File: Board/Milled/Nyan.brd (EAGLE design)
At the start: 86 x 42 mm, 21 parts, among them IC1 74HCT541N, T1 TSM2314CX, U1 BLUEPILL455, U2 A4988_STEP, U3 MAX6966, X1 WR-WTB2.0-2_THT-VER, X2 WR-WTB2.0-4_THT_VER, X3 WR-WTB2.0-4_THT_VER, X4 WR-WTB2.0-5_THT-VER, X6 68610614122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

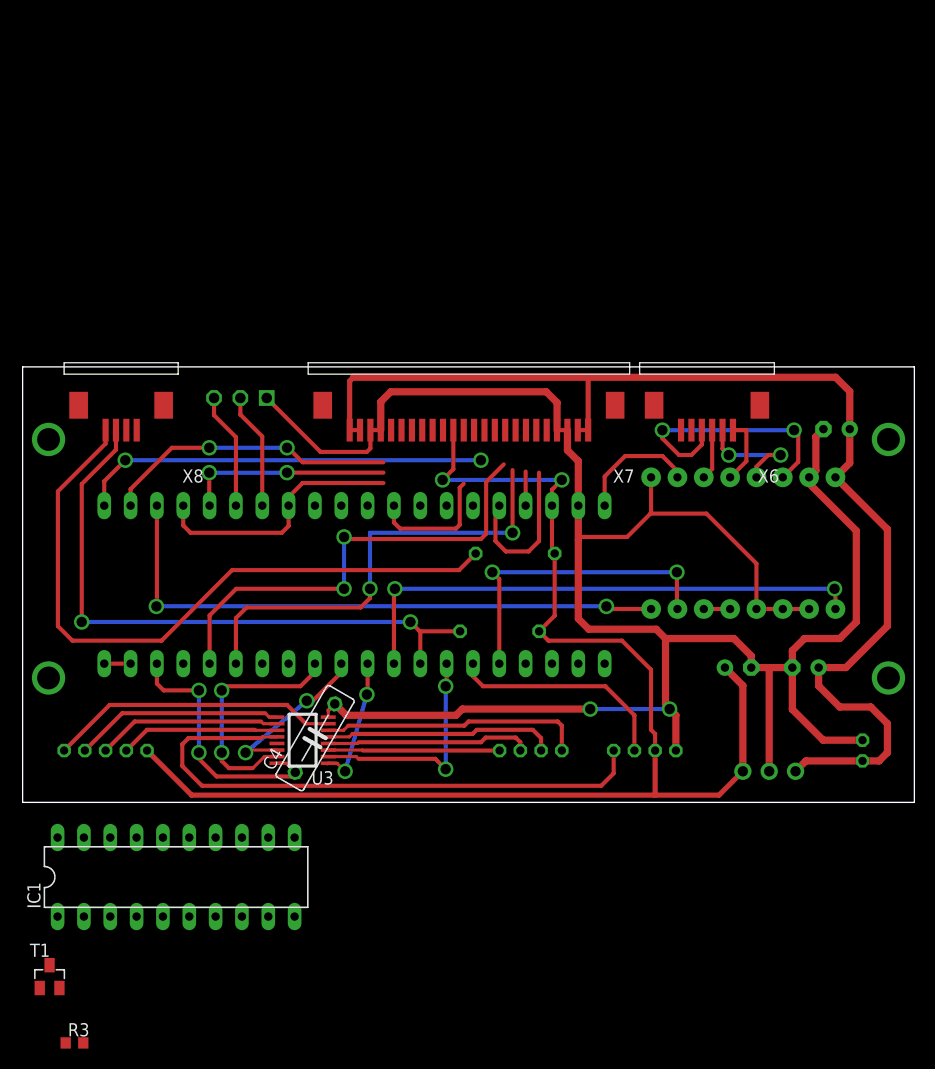
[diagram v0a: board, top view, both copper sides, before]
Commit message: Current development state with hardware fixes for 3 to 5 volt level shifting
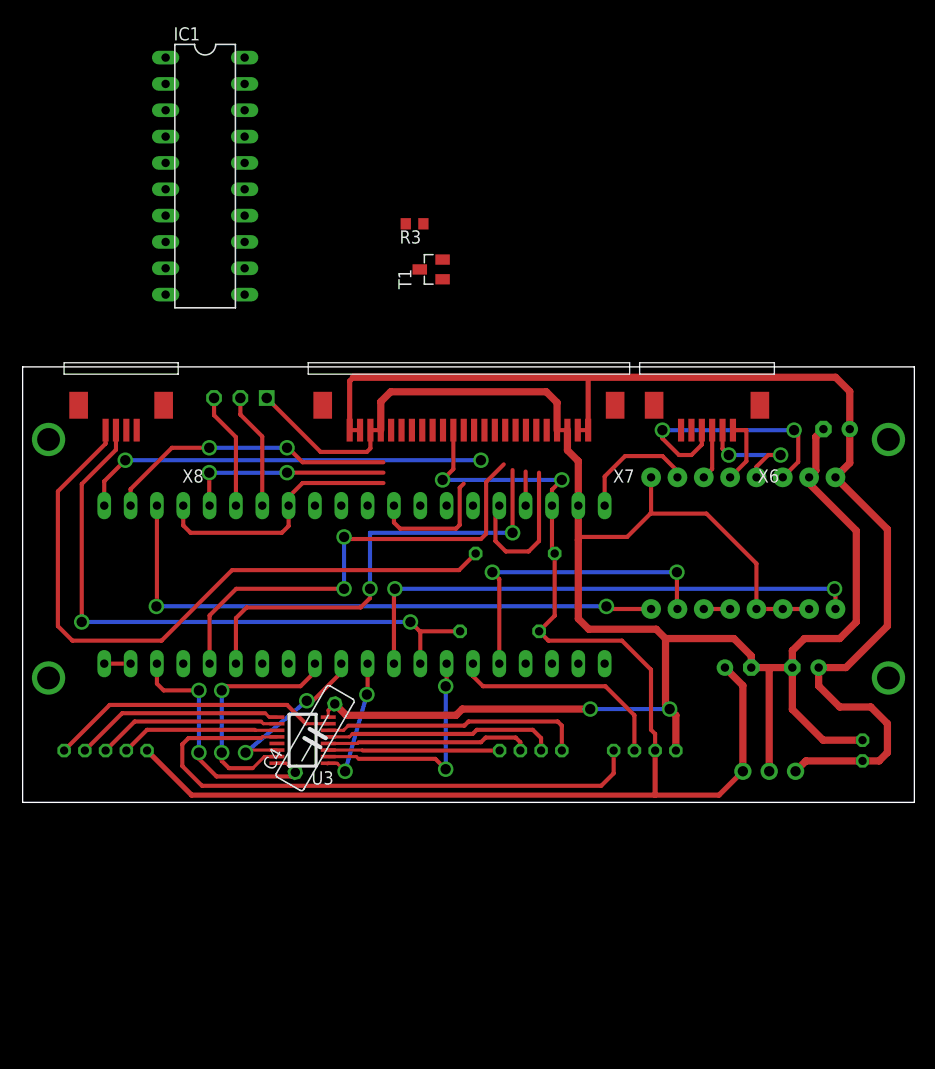
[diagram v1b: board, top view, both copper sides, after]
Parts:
- moved R3 85.5 mm to (37.8, 55.8), turned to 180 degrees
- moved T1 77.5 mm to (39.4, 51.4), turned to 90 degrees
- moved IC1 67.7 mm to (17.6, 60.4), turned to 270 degrees
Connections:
- removed net N$10: IC1.18
- removed net N$11: IC1.17
- removed net N$12: IC1.16
- removed net N$13: IC1.15
- removed net N$14: IC1.14
- removed net N$15: IC1.13
- removed net N$16: IC1.12
- removed net N$17: IC1.11
- removed net N$18: IC1.2
- removed net N$19: IC1.3
- removed net N$20: IC1.4
- removed net N$21: IC1.5
- removed net N$22: IC1.6
- removed net N$23: IC1.7
- removed net N$24: IC1.8
- removed net N$25: IC1.9
- removed net N$8: R3.1, T1.3
- removed net N$9: T1.1
- net D1: now also IC1.2
- net D1_5V: now also IC1.18
- net D2: now also IC1.3
- net D2_5V: now also IC1.17
- net D3: now also IC1.4
- net D3_5V: now also IC1.16
- net D4: now also IC1.5
- net D4_5V: now also IC1.15
- net D5: now also IC1.6
- net D5_5V: now also IC1.14
- net D6: now also IC1.7
- net D6_5V: now also IC1.13
- net DCLK: now also IC1.8
- net DCLK_5V: now also IC1.12
- net LATCH: now also T1.1
- net LATCH_5V: now also R3.1, T1.3
- net STROBE: now also IC1.9
- net STROBE_5V: now also IC1.11
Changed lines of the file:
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@@
 <element name="R1" library="rcl" package="0204/7" value="300" x="47.5" y="24" locked="yes" rot="MR180"/>
 <element name="R2" library="rcl" package="0204/7" value="47k" x="46" y="16.5" locked="yes" rot="MR180"/>
-<element name="IC1" library="74xx-eu" package="DIL20" value="74HCT541N" x="14.8" y="-7.2"/>
-<element name="T1" library="TURAG_Mosfet_N-Kanal" package="SOT-23" value="TSM2314CX" x="2.6" y="-16.8">
-<attribute name="FARNELL" value="1864589" x="2.6" y="-16.8" size="1.778" layer="27" display="off"/>
+<element name="IC1" library="74xx-eu" package="DIL20" value="74HCT541N" x="17.6" y="60.4" rot="R270"/>
+<element name="T1" library="TURAG_Mosfet_N-Kanal" package="SOT-23" value="TSM2314CX" x="39.4" y="51.4" rot="R90">
+<attribute name="FARNELL" value="1864589" x="39.4" y="51.4" size="1.778" layer="27" rot="R90" display="off"/>
 </element>
-<element name="R3" library="rcl" package="R0603" value="10k" x="5" y="-23.2"/>
+<element name="R3" library="rcl" package="R0603" value="10k" x="37.8" y="55.8" rot="R180"/>
 </elements>
 <signals>
@@
 <contactref element="IC1" pad="10"/>
 <contactref element="T1" pad="2"/>
-<wire x1="26.23" y1="-11.01" x2="29.475" y2="8.2225" width="0" layer="19" extent="1-1"/>
+<wire x1="13.79" y1="48.97" x2="29.475" y2="8.2225" width="0" layer="19" extent="1-1"/>
 <wire x1="10.41" y1="13.38" x2="29.475" y2="8.86955625" width="0" layer="19" extent="1-1"/>
-<wire x1="5.91" y1="-3.39" x2="7.87" y2="13.38" width="0" layer="19" extent="1-1"/>
-<wire x1="3.37" y1="-11.01" x2="5.91" y2="-3.39" width="0" layer="19" extent="1-1"/>
-<wire x1="3.55" y1="-17.9" x2="3.37" y2="-11.01" width="0" layer="19" extent="1-1"/>
+<wire x1="21.41" y1="69.29" x2="7.87" y2="13.38" width="0" layer="19" extent="1-1"/>
+<wire x1="13.79" y1="71.83" x2="21.41" y2="69.29" width="0" layer="19" extent="1-1"/>
+<wire x1="40.5" y1="52.35" x2="13.79" y2="71.83" width="0" layer="19" extent="1-1"/>
 </signal>
 <signal name="+5V">
@@
 <contactref element="IC1" pad="20"/>
 <contactref element="R3" pad="2"/>
-<wire x1="3.37" y1="-3.39" x2="5.85" y2="-23.2" width="0" layer="19" extent="1-1"/>
-<wire x1="12" y1="5" x2="3.37" y2="-3.39" width="0" layer="19" extent="1-1"/>
+<wire x1="21.41" y1="71.83" x2="36.95" y2="55.8" width="0" layer="19" extent="1-1"/>
+<wire x1="12" y1="5" x2="21.41" y2="71.83" width="0" layer="19" extent="1-1"/>
 </signal>
 <signal name="+12V">
@@
 <wire x1="47.25" y1="26" x2="33.5" y2="26" width="0.4" layer="16"/>
 <wire x1="33.5" y1="26" x2="33.5" y2="20.6" width="0.4" layer="16"/>
+<contactref element="IC1" pad="4"/>
+<wire x1="13.79" y1="64.21" x2="20.57" y2="13.38" width="0" layer="19" extent="1-1"/>
 </signal>
 <signal name="D4">
@@
 <wire x1="31.2" y1="25.4" x2="31" y2="25.6" width="0.4" layer="1"/>
 <wire x1="44.7" y1="30.9" x2="46.4" y2="32.6" width="0.4" layer="1"/>
+<contactref element="IC1" pad="5"/>
+<wire x1="13.79" y1="61.67" x2="18.03" y2="13.38" width="0" layer="19" extent="1-1"/>
 </signal>
 <signal name="D1">
@@
 <wire x1="48.8" y1="24.2" x2="49.8" y2="25.2" width="0.4" layer="1"/>
 <wire x1="49.8" y1="25.2" x2="49.8" y2="31.8" width="0.4" layer="1"/>
+<contactref element="IC1" pad="2"/>
+<wire x1="13.79" y1="69.29" x2="45.6" y2="25.2" width="0" layer="19" extent="1-1"/>
 </signal>
 <signal name="D2">
 <contactref element="U1" pad="37"/>
 <wire x1="48.51" y1="31.91" x2="48.51" y2="28.62" width="0.4" layer="1"/>
+<contactref element="IC1" pad="3"/>
+<wire x1="13.79" y1="66.75" x2="48.51" y2="28.62" width="0" layer="19" extent="1-1"/>
 </signal>
 <signal name="D5">
@@
 <wire x1="9.9" y1="33" x2="7.87" y2="30.97" width="0.4" layer="1"/>
 <wire x1="7.87" y1="30.97" x2="7.87" y2="28.62" width="0.4" layer="1"/>
+<contactref element="IC1" pad="6"/>
+<wire x1="13.79" y1="59.13" x2="7.87" y2="28.62" width="0" layer="19" extent="1-1"/>
 </signal>
 <signal name="D6">
@@
 <wire x1="14.4" y1="34.2" x2="10.41" y2="30.21" width="0.4" layer="1"/>
 <wire x1="10.41" y1="30.21" x2="10.41" y2="28.62" width="0.4" layer="1"/>
+<contactref element="IC1" pad="7"/>
+<wire x1="13.79" y1="56.59" x2="10.41" y2="28.62" width="0" layer="19" extent="1-1"/>
 </signal>
 <signal name="USART_TX">
@@
 <wire x1="36.4" y1="26.4" x2="35.81" y2="26.99" width="0.4" layer="1"/>
 <wire x1="35.81" y1="26.99" x2="35.81" y2="28.62" width="0.4" layer="1"/>
+<contactref element="IC1" pad="9"/>
+<wire x1="13.79" y1="51.51" x2="36.4" y2="26.4" width="0" layer="19" extent="1-1"/>
 </signal>
 <signal name="N$1">
@@
 <wire x1="16.2" y1="26" x2="15.49" y2="26.71" width="0.4" layer="1"/>
 <wire x1="15.49" y1="26.71" x2="15.49" y2="28.62" width="0.4" layer="1"/>
+<contactref element="T1" pad="1"/>
+<wire x1="40.5" y1="50.45" x2="16.2" y2="26" width="0" layer="19" extent="1-1"/>
 </signal>
 <signal name="DCLK">
@@
 <wire x1="18" y1="28.65" x2="18.03" y2="28.62" width="0.4" layer="1"/>
 <wire x1="34.8" y1="31.8" x2="25.5" y2="31.8" width="0.4" layer="1"/>
+<contactref element="IC1" pad="8"/>
+<wire x1="13.79" y1="54.05" x2="18.03" y2="28.62" width="0" layer="19" extent="1-1"/>
 </signal>
 <signal name="N$3">
@@
 <via x="2.5" y="35" extent="1-16" drill="2.2"/>
 </signal>
-<signal name="N$8">
+<signal name="D1_5V">
+<contactref element="X7" pad="5"/>
+<contactref element="IC1" pad="18"/>
+<wire x1="21.41" y1="66.75" x2="50.54" y2="35.9" width="0" layer="19" extent="1-1"/>
+</signal>
+<signal name="D2_5V">
+<contactref element="X7" pad="6"/>
+<contactref element="IC1" pad="17"/>
+<wire x1="21.41" y1="64.21" x2="49.54" y2="35.9" width="0" layer="19" extent="1-1"/>
+</signal>
+<signal name="D3_5V">
+<contactref element="X7" pad="7"/>
+<contactref element="IC1" pad="16"/>
+<wire x1="21.41" y1="61.67" x2="48.54" y2="35.9" width="0" layer="19" extent="1-1"/>
+</signal>
+<signal name="D4_5V">
+<contactref element="X7" pad="8"/>
+<contactref element="IC1" pad="15"/>
+<wire x1="21.41" y1="59.13" x2="47.54" y2="35.9" width="0" layer="19" extent="1-1"/>
+</signal>
+<signal name="D5_5V">
+<contactref element="X7" pad="9"/>
+<contactref element="IC1" pad="14"/>
+<wire x1="21.41" y1="56.59" x2="46.54" y2="35.9" width="0" layer="19" extent="1-1"/>
+</signal>
+<signal name="STROBE_5V">
+<contactref element="X7" pad="13"/>
+<contactref element="IC1" pad="11"/>
+<wire x1="21.41" y1="48.97" x2="42.54" y2="35.9" width="0" layer="19" extent="1-1"/>
+</signal>
+<signal name="LATCH_5V">
+<contactref element="X7" pad="15"/>
 <contactref element="R3" pad="1"/>
 <contactref element="T1" pad="3"/>
-<wire x1="2.6" y1="-15.7" x2="4.15" y2="-23.2" width="0" layer="19" extent="1-1"/>
-</signal>
-<signal name="N$9">
-<contactref element="T1" pad="1"/>
-</signal>
-<signal name="N$10">
-<contactref element="IC1" pad="18"/>
-</signal>
-<signal name="N$11">
-<contactref element="IC1" pad="17"/>
-</signal>
-<signal name="N$12">
-<contactref element="IC1" pad="16"/>
-</signal>
-<signal name="N$13">
-<contactref element="IC1" pad="15"/>
-</signal>
-<signal name="N$14">
-<contactref element="IC1" pad="14"/>
-</signal>
-<signal name="N$15">
-<contactref element="IC1" pad="13"/>
-</signal>
-<signal name="N$16">
-<contactref element="IC1" pad="12"/>
-</signal>
-<signal name="N$17">
-<contactref element="IC1" pad="11"/>
-</signal>
-<signal name="N$18">
-<contactref element="IC1" pad="2"/>
-</signal>
-<signal name="N$19">
-<contactref element="IC1" pad="3"/>
-</signal>
-<signal name="N$20">
-<contactref element="IC1" pad="4"/>
-</signal>
-<signal name="N$21">
-<contactref element="IC1" pad="5"/>
-</signal>
-<signal name="N$22">
-<contactref element="IC1" pad="6"/>
-</signal>
-<signal name="N$23">
-<contactref element="IC1" pad="7"/>
-</signal>
-<signal name="N$24">
-<contactref element="IC1" pad="8"/>
-</signal>
-<signal name="N$25">
-<contactref element="IC1" pad="9"/>
-</signal>
-<signal name="D1_5V">
-<contactref element="X7" pad="5"/>
-</signal>
-<signal name="D2_5V">
-<contactref element="X7" pad="6"/>
-</signal>
-<signal name="D3_5V">
-<contactref element="X7" pad="7"/>
-</signal>
-<signal name="D4_5V">
-<contactref element="X7" pad="8"/>
-</signal>
-<signal name="D5_5V">
-<contactref element="X7" pad="9"/>
-</signal>
-<signal name="STROBE_5V">
-<contactref element="X7" pad="13"/>
-</signal>
-<signal name="LATCH_5V">
-<contactref element="X7" pad="15"/>
+<wire x1="38.3" y1="51.4" x2="40.54" y2="35.9" width="0" layer="19" extent="1-1"/>
+<wire x1="38.65" y1="55.8" x2="38.3" y2="51.4" width="0" layer="19" extent="1-1"/>
 </signal>
 <signal name="DCLK_5V">
 <contactref element="X7" pad="16"/>
+<contactref element="IC1" pad="12"/>
+<wire x1="21.41" y1="51.51" x2="39.54" y2="35.9" width="0" layer="19" extent="1-1"/>
 </signal>
 <signal name="D6_5V">
 <contactref element="X7" pad="17"/>
+<contactref element="IC1" pad="13"/>
+<wire x1="21.41" y1="54.05" x2="38.54" y2="35.9" width="0" layer="19" extent="1-1"/>
 </signal>
 </signals>
